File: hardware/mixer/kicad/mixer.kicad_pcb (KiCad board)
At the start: 2 copper layers, 34.3 x 22.9 mm, 5 parts, among them J1 SMA-J-P-H-ST-TH1, J2 SMA-J-P-H-ST-TH1, J3 SMA-J-P-H-ST-TH1, U1 HMC787ALC3BTR

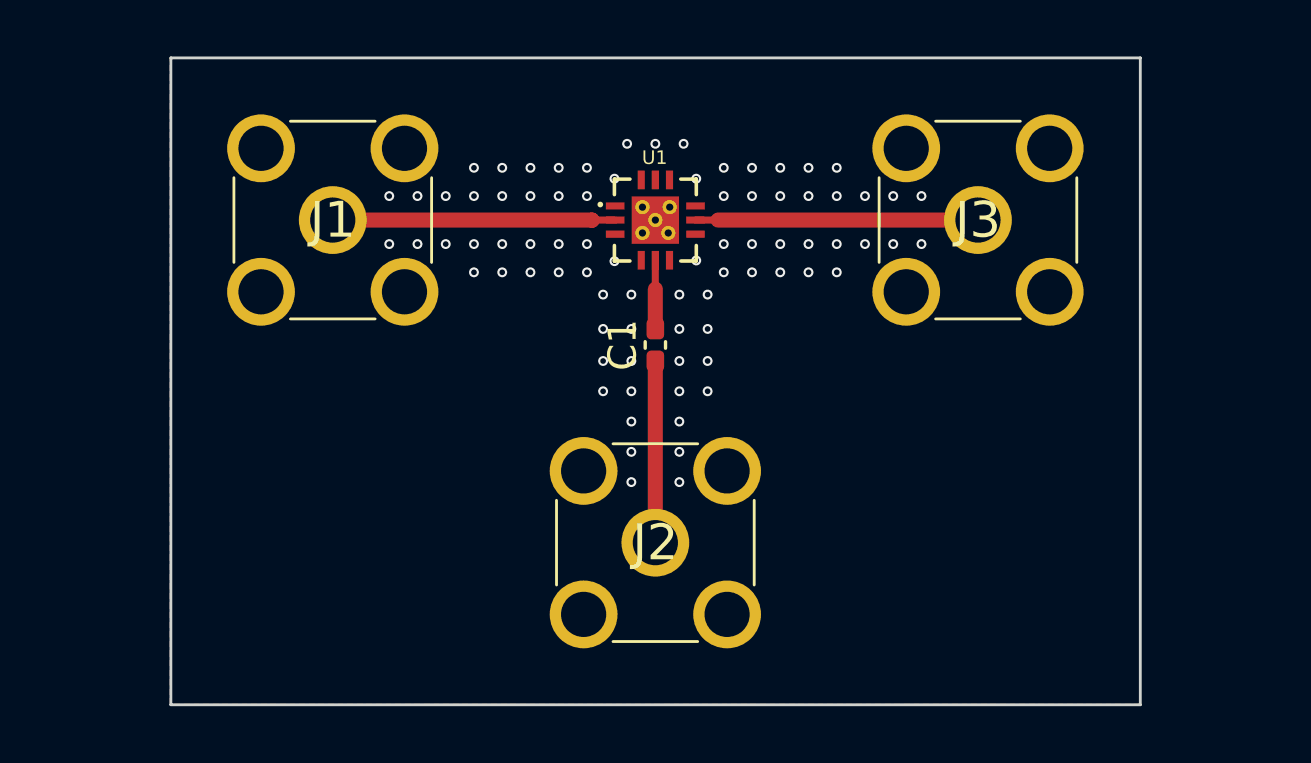
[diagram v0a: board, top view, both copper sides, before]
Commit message: Add mixer footprint and symbols
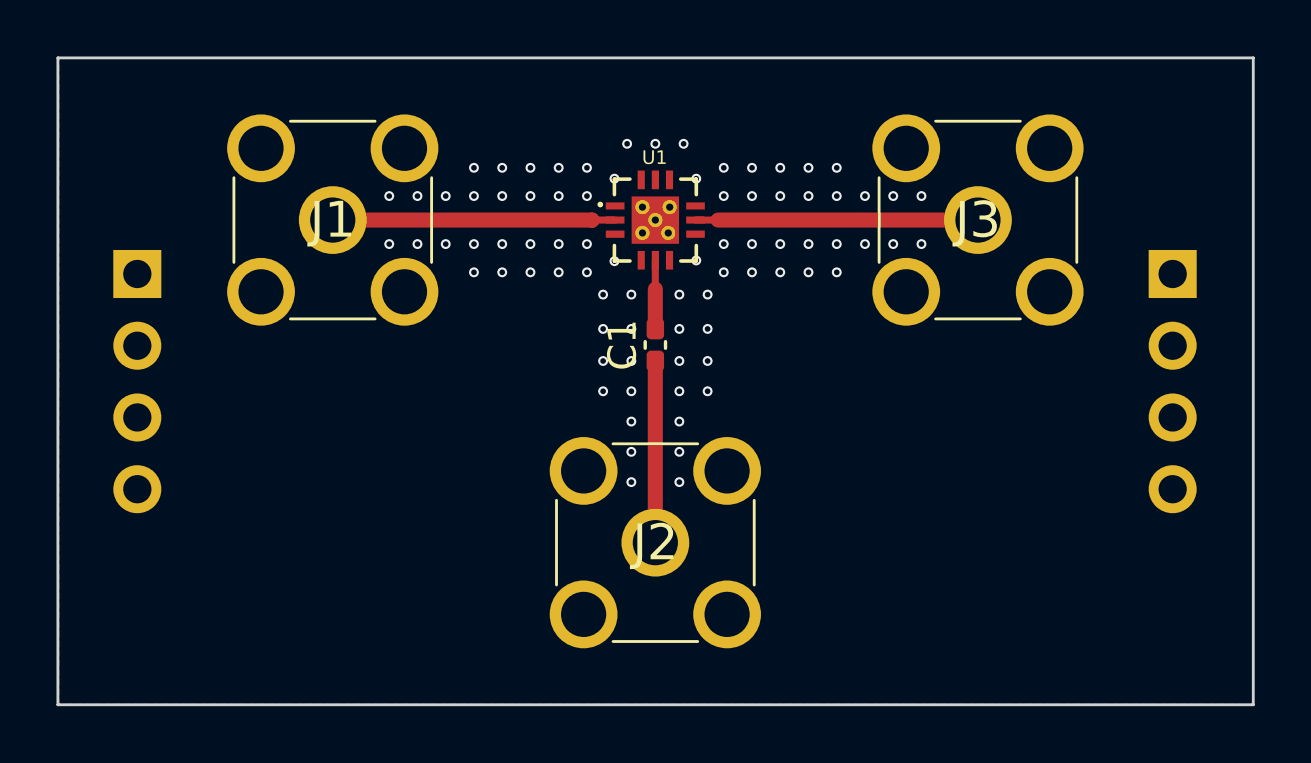
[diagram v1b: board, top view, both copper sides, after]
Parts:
- added J4: Conn_01x04, Connector_PinHeader_2.54mm:PinHeader_1x04_P2.54mm_Vertical, B.Cu at (110.8, 75.9)
- added J5: Conn_01x04, Connector_PinHeader_2.54mm:PinHeader_1x04_P2.54mm_Vertical, B.Cu at (147.5, 75.9)
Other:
- board size 34.3 x 22.9 mm -> 42.3 x 22.9 mm
